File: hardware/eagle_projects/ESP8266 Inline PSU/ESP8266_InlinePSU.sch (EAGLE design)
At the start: 1 part

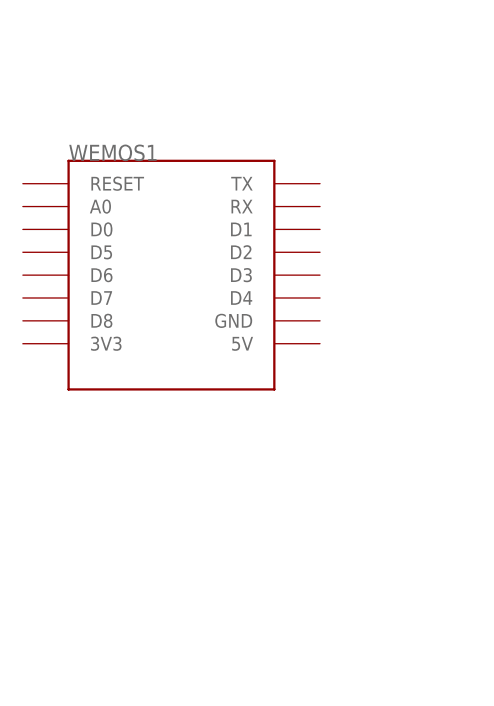
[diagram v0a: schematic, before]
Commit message: Beginning build process for wireless inline PSU and modifications of PSU
Signed-off-by: Braden Licastro <blicastro@live.com>
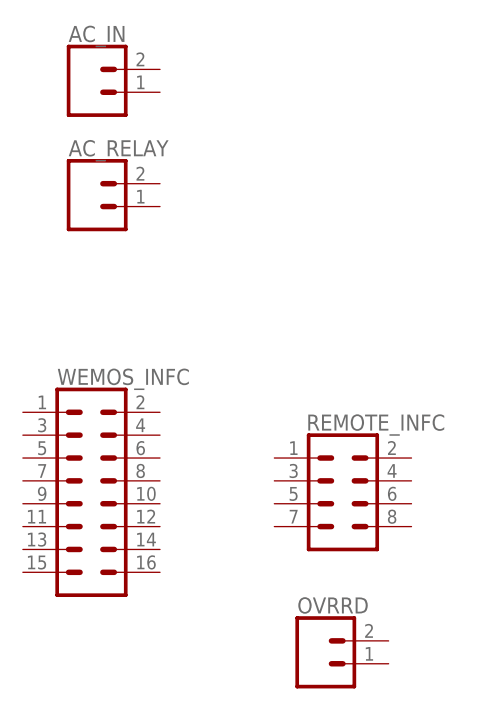
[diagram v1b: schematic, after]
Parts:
- removed WEMOS1: (no value), esp8266modules:WEMOS-D1-MINI
- added AC_IN, AC_RELAY: (no value), SparkFun-Connectors:CONN_023.5MM_LOCK
- added OVRRD: (no value), SparkFun-Connectors:CONN_02LOCK
- added REMOTE_INFC: (no value), SparkFun-Connectors:CONN_04X2
- added WEMOS_INFC: (no value), SparkFun-Connectors:CONN_08X2

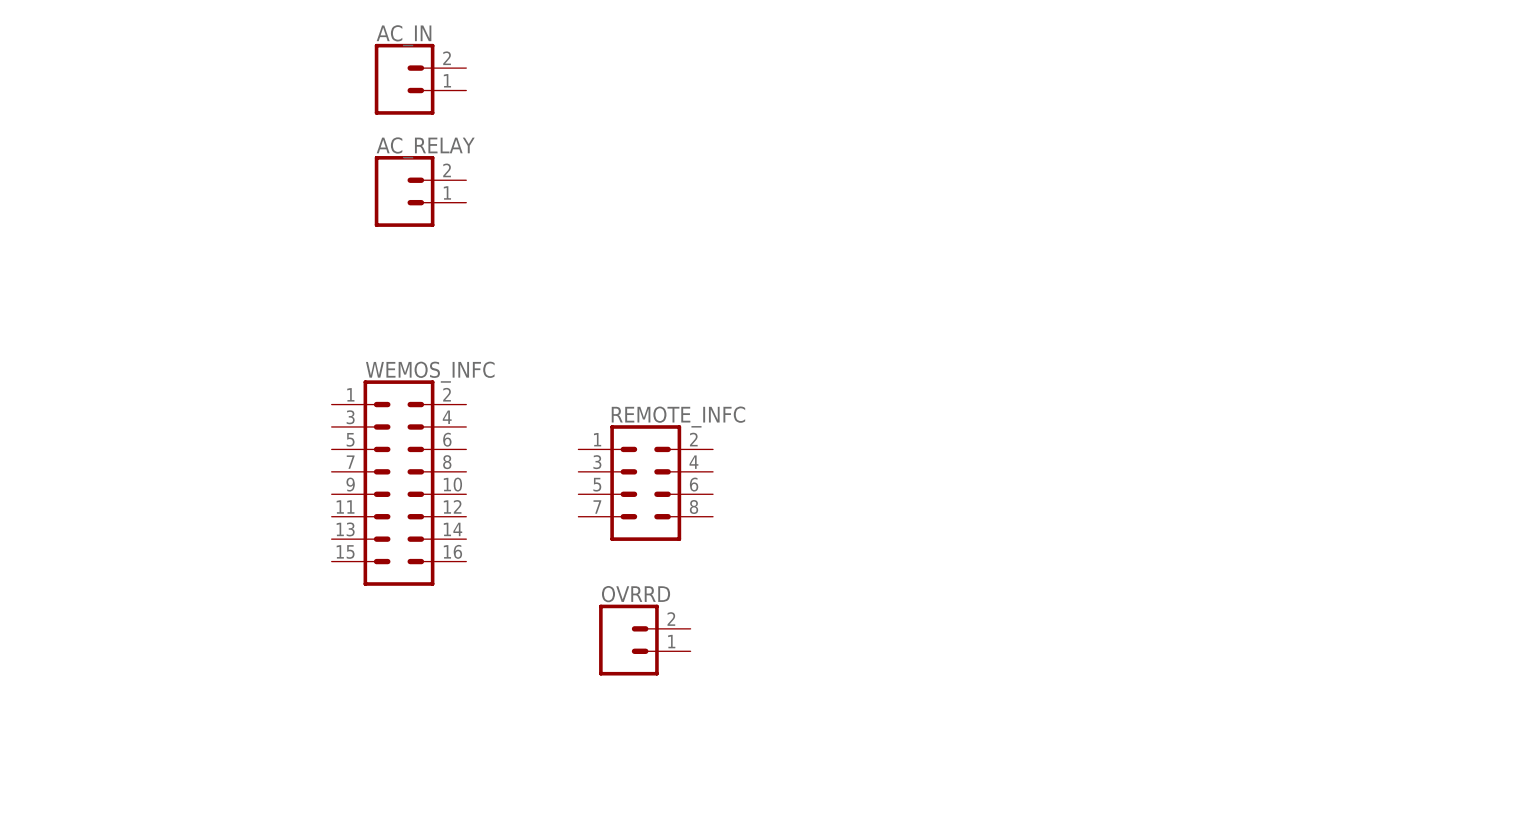
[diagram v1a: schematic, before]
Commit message: Completed more work on hardware design. Broke out sections of sensitive code, optimised existing code. Hacked new device for use and built new firmware. Updated test firmware for deployment on multiple ESP devices.
Signed-off-by: Braden Licastro <blicastro@live.com>
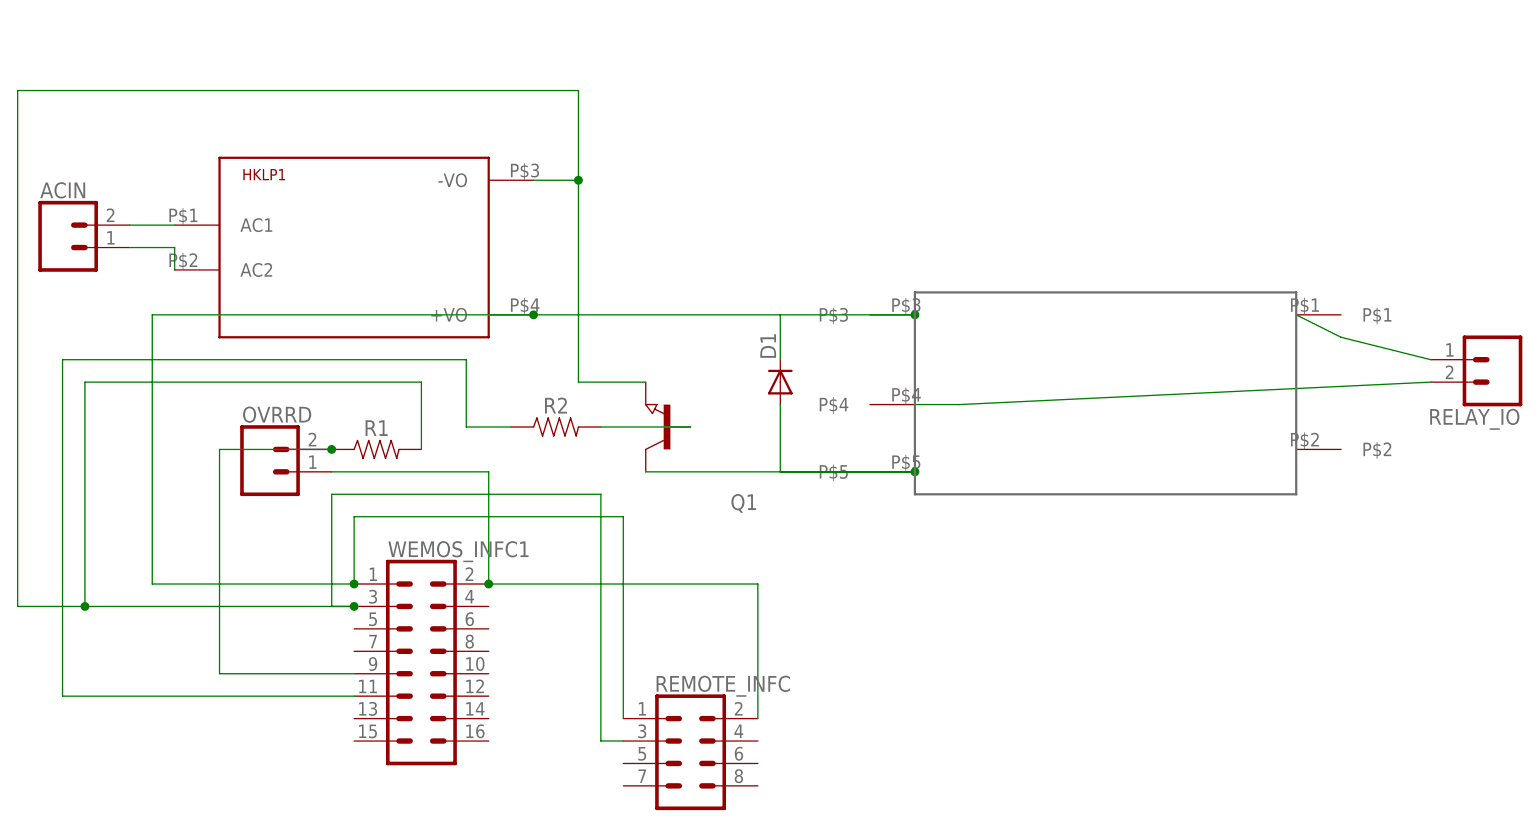
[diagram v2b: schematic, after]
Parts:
- removed AC_IN, AC_RELAY: (no value), SparkFun-Connectors:CONN_023.5MM_LOCK
- removed WEMOS_INFC: (no value), SparkFun-Connectors:CONN_08X2
- added ACIN, RELAY_IO: (no value), SparkFun-Connectors:CONN_025MM
- added D1: 1N4148DO35-7, diode:1N4148DO35-7
- added HKLP1: HKLPM01, bl_components:HKLPM01
- added Q1: (no value), semicon-smd-ipc:NPN-TRANSISTOR_SOT23
- added R1, R2: (no value), SparkFun-Resistors:RESISTOR0805
- added U$1: SRD-05VDC-SL-CTH, bl_components:SRD-05VDC-SL-CTH
- added WEMOS_INFC1: (no value), SparkFun-Connectors:CONN_08X2
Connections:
- new net N$1: ACIN.2, HKLP1.AC1
- new net N$10: Q1.B, R2.2
- new net N$11: R2.1, WEMOS_INFC1.11
- new net N$2: ACIN.1, HKLP1.AC2
- new net N$3: D1.C, HKLP1.+VO, REMOTE_INFC.1, U$1.P$3, WEMOS_INFC1.1
- new net N$4: OVRRD.1, REMOTE_INFC.2, WEMOS_INFC1.2
- new net N$5: HKLP1.-VO, Q1.E, R1.2, REMOTE_INFC.3, WEMOS_INFC1.3
- new net N$6: RELAY_IO.1, U$1.P$1
- new net N$7: RELAY_IO.2, U$1.P$4
- new net N$8: D1.A, Q1.C, U$1.P$5
- new net N$9: OVRRD.2, R1.1, WEMOS_INFC1.9
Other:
- moved on the sheet: OVRRD, REMOTE_INFC
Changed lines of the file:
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@@
 <?xml version="1.0" encoding="utf-8"?>
 <!DOCTYPE eagle SYSTEM "eagle.dtd">
-<eagle version="8.4.0">
+<eagle version="8.4.3">
 <drawing>
 <settings>
@@
 </classes>
 <parts>
-<part name="WEMOS_INFC" library="SparkFun-Connectors" library_urn="urn:adsk.eagle:library:513" deviceset="CONN_08X2" device="" package3d_urn="urn:adsk.eagle:package:38152/1"/>
 <part name="REMOTE_INFC" library="SparkFun-Connectors" library_urn="urn:adsk.eagle:library:513" deviceset="CONN_04X2" device="" package3d_urn="urn:adsk.eagle:package:38103/1"/>
 <part name="OVRRD" library="SparkFun-Connectors" library_urn="urn:adsk.eagle:library:513" deviceset="CONN_02" device="LOCK" package3d_urn="urn:adsk.eagle:package:38045/1"/>
-<part name="AC_IN" library="SparkFun-Connectors" library_urn="urn:adsk.eagle:library:513" deviceset="CONN_02" device="3.5MM_LOCK" package3d_urn="urn:adsk.eagle:package:38049/1"/>
-<part name="AC_RELAY" library="SparkFun-Connectors" library_urn="urn:adsk.eagle:library:513" deviceset="CONN_02" device="3.5MM_LOCK" package3d_urn="urn:adsk.eagle:package:38049/1"/>
+<part name="WEMOS_INFC1" library="SparkFun-Connectors" library_urn="urn:adsk.eagle:library:513" deviceset="CONN_08X2" device="" package3d_urn="urn:adsk.eagle:package:38152/1"/>
+<part name="HKLP1" library="bl_components" deviceset="HKLPM01" device=""/>
+<part name="U$1" library="bl_components" deviceset="SRD-05VDC-SL-C" device="TH"/>
+<part name="RELAY_IO" library="SparkFun-Connectors" library_urn="urn:adsk.eagle:library:513" deviceset="CONN_02" device="5MM" package3d_urn="urn:adsk.eagle:package:38044/1"/>
+<part name="ACIN" library="SparkFun-Connectors" library_urn="urn:adsk.eagle:library:513" deviceset="CONN_02" device="5MM" package3d_urn="urn:adsk.eagle:package:38044/1"/>
+<part name="R1" library="SparkFun-Resistors" deviceset="RESISTOR" device="0805" value=" "/>
+<part name="D1" library="diode" library_urn="urn:adsk.eagle:library:210" deviceset="1N4148" device="DO35-7" package3d_urn="urn:adsk.eagle:package:43339/1"/>
+<part name="Q1" library="semicon-smd-ipc" library_urn="urn:adsk.eagle:library:353" deviceset="NPN-TRANSISTOR_" device="SOT23" package3d_urn="urn:adsk.eagle:package:26310/1"/>
+<part name="R2" library="SparkFun-Resistors" deviceset="RESISTOR" device="0805" value=" "/>
 </parts>
 <sheets>
@@
 </plain>
 <instances>
-<instance part="WEMOS_INFC" gate="G$1" x="78.74" y="45.72"/>
-<instance part="REMOTE_INFC" gate="G$1" x="106.68" y="45.72"/>
-<instance part="OVRRD" gate="G$1" x="104.14" y="27.94"/>
-<instance part="AC_IN" gate="G$1" x="78.74" y="91.44"/>
-<instance part="AC_RELAY" gate="G$1" x="78.74" y="78.74"/>
+<instance part="REMOTE_INFC" gate="G$1" x="111.76" y="15.24"/>
+<instance part="OVRRD" gate="G$1" x="63.5" y="48.26"/>
+<instance part="WEMOS_INFC1" gate="G$1" x="81.28" y="25.4"/>
+<instance part="HKLP1" gate="G$1" x="73.66" y="73.66"/>
+<instance part="U$1" gate="G$1" x="137.16" y="45.72"/>
+<instance part="RELAY_IO" gate="G$1" x="203.2" y="60.96" rot="R180"/>
+<instance part="ACIN" gate="G$1" x="40.64" y="73.66"/>
+<instance part="R1" gate="G$1" x="76.2" y="50.8"/>
+<instance part="D1" gate="G$1" x="121.92" y="58.42" smashed="yes" rot="R90">
+<attribute name="NAME" x="121.4374" y="60.96" size="1.778" layer="95" rot="R90"/>
+</instance>
+<instance part="Q1" gate="G$1" x="109.22" y="53.34" rot="R180"/>
+<instance part="R2" gate="G$1" x="96.52" y="53.34"/>
 </instances>
 <busses>
 </busses>
 <nets>
+<net name="N$1" class="0">
+<segment>
+<pinref part="ACIN" gate="G$1" pin="2"/>
+<pinref part="HKLP1" gate="G$1" pin="AC1"/>
+<wire x1="48.26" y1="76.2" x2="53.34" y2="76.2" width="0.1524" layer="91"/>
+</segment>
+</net>
+<net name="N$2" class="0">
+<segment>
+<pinref part="ACIN" gate="G$1" pin="1"/>
+<pinref part="HKLP1" gate="G$1" pin="AC2"/>
+<wire x1="48.26" y1="73.66" x2="53.34" y2="73.66" width="0.1524" layer="91"/>
+<wire x1="53.34" y1="73.66" x2="53.34" y2="71.12" width="0.1524" layer="91"/>
+</segment>
+</net>
+<net name="N$3" class="0">
+<segment>
+<pinref part="WEMOS_INFC1" gate="G$1" pin="1"/>
+<wire x1="73.66" y1="35.56" x2="73.66" y2="43.18" width="0.1524" layer="91"/>
+<pinref part="REMOTE_INFC" gate="G$1" pin="1"/>
+<wire x1="73.66" y1="43.18" x2="104.14" y2="43.18" width="0.1524" layer="91"/>
+<wire x1="104.14" y1="43.18" x2="104.14" y2="20.32" width="0.1524" layer="91"/>
+<pinref part="HKLP1" gate="G$1" pin="+VO"/>
+<wire x1="93.98" y1="66.04" x2="50.8" y2="66.04" width="0.1524" layer="91"/>
+<wire x1="50.8" y1="66.04" x2="50.8" y2="35.56" width="0.1524" layer="91"/>
+<wire x1="50.8" y1="35.56" x2="73.66" y2="35.56" width="0.1524" layer="91"/>
+<junction x="73.66" y="35.56"/>
+<pinref part="U$1" gate="G$1" pin="P$3"/>
+<wire x1="93.98" y1="66.04" x2="121.92" y2="66.04" width="0.1524" layer="91"/>
+<junction x="93.98" y="66.04"/>
+<pinref part="D1" gate="G$1" pin="C"/>
+<wire x1="137.16" y1="66.04" x2="121.92" y2="66.04" width="0.1524" layer="91"/>
+<wire x1="121.92" y1="66.04" x2="121.92" y2="60.96" width="0.1524" layer="91"/>
+<junction x="137.16" y="66.04"/>
+</segment>
+</net>
+<net name="N$4" class="0">
+<segment>
+<pinref part="WEMOS_INFC1" gate="G$1" pin="2"/>
+<pinref part="REMOTE_INFC" gate="G$1" pin="2"/>
+<wire x1="88.9" y1="35.56" x2="119.38" y2="35.56" width="0.1524" layer="91"/>
+<wire x1="119.38" y1="35.56" x2="119.38" y2="20.32" width="0.1524" layer="91"/>
+<pinref part="OVRRD" gate="G$1" pin="1"/>
+<wire x1="71.12" y1="48.26" x2="88.9" y2="48.26" width="0.1524" layer="91"/>
+<wire x1="88.9" y1="48.26" x2="88.9" y2="35.56" width="0.1524" layer="91"/>
+<junction x="88.9" y="35.56"/>
+</segment>
+</net>
+<net name="N$5" class="0">
+<segment>
+<pinref part="WEMOS_INFC1" gate="G$1" pin="3"/>
+<wire x1="73.66" y1="33.02" x2="71.12" y2="33.02" width="0.1524" layer="91"/>
+<wire x1="71.12" y1="33.02" x2="71.12" y2="45.72" width="0.1524" layer="91"/>
+<wire x1="71.12" y1="45.72" x2="101.6" y2="45.72" width="0.1524" layer="91"/>
+<wire x1="101.6" y1="45.72" x2="101.6" y2="17.78" width="0.1524" layer="91"/>
+<pinref part="REMOTE_INFC" gate="G$1" pin="3"/>
+<wire x1="101.6" y1="17.78" x2="104.14" y2="17.78" width="0.1524" layer="91"/>
+<pinref part="HKLP1" gate="G$1" pin="-VO"/>
+<wire x1="93.98" y1="81.28" x2="99.06" y2="81.28" width="0.1524" layer="91"/>
+<wire x1="99.06" y1="81.28" x2="99.06" y2="91.44" width="0.1524" layer="91"/>
+<wire x1="99.06" y1="91.44" x2="35.56" y2="91.44" width="0.1524" layer="91"/>
+<wire x1="35.56" y1="91.44" x2="35.56" y2="33.02" width="0.1524" layer="91"/>
+<wire x1="35.56" y1="33.02" x2="43.18" y2="33.02" width="0.1524" layer="91"/>
+<junction x="73.66" y="33.02"/>
+<pinref part="R1" gate="G$1" pin="2"/>
+<wire x1="43.18" y1="33.02" x2="73.66" y2="33.02" width="0.1524" layer="91"/>
+<wire x1="81.28" y1="50.8" x2="81.28" y2="58.42" width="0.1524" layer="91"/>
+<wire x1="81.28" y1="58.42" x2="43.18" y2="58.42" width="0.1524" layer="91"/>
+<wire x1="43.18" y1="58.42" x2="43.18" y2="33.02" width="0.1524" layer="91"/>
+<junction x="43.18" y="33.02"/>
+<pinref part="Q1" gate="G$1" pin="E"/>
+<wire x1="106.68" y1="58.42" x2="99.06" y2="58.42" width="0.1524" layer="91"/>
+<wire x1="99.06" y1="58.42" x2="99.06" y2="81.28" width="0.1524" layer="91"/>
+<junction x="99.06" y="81.28"/>
+</segment>
+</net>
+<net name="N$9" class="0">
+<segment>
+<pinref part="OVRRD" gate="G$1" pin="2"/>
+<wire x1="71.12" y1="50.8" x2="58.42" y2="50.8" width="0.1524" layer="91"/>
+<wire x1="58.42" y1="50.8" x2="58.42" y2="25.4" width="0.1524" layer="91"/>
+<pinref part="WEMOS_INFC1" gate="G$1" pin="9"/>
+<wire x1="58.42" y1="25.4" x2="73.66" y2="25.4" width="0.1524" layer="91"/>
+<pinref part="R1" gate="G$1" pin="1"/>
+<junction x="71.12" y="50.8"/>
+</segment>
+</net>
+<net name="N$6" class="0">
+<segment>
+<pinref part="RELAY_IO" gate="G$1" pin="1"/>
+<pinref part="U$1" gate="G$1" pin="P$1"/>
+<wire x1="195.58" y1="60.96" x2="185.42" y2="63.5" width="0.1524" layer="91"/>
+<wire x1="185.42" y1="63.5" x2="180.34" y2="66.04" width="0.1524" layer="91"/>
+</segment>
+</net>
+<net name="N$7" class="0">
+<segment>
+<pinref part="U$1" gate="G$1" pin="P$4"/>
+<pinref part="RELAY_IO" gate="G$1" pin="2"/>
+<wire x1="137.16" y1="55.88" x2="142.24" y2="55.88" width="0.1524" layer="91"/>
+<wire x1="142.24" y1="55.88" x2="195.58" y2="58.42" width="0.1524" layer="91"/>
+</segment>
+</net>
+<net name="N$8" class="0">
+<segment>
+<pinref part="U$1" gate="G$1" pin="P$5"/>
+<pinref part="D1" gate="G$1" pin="A"/>
+<wire x1="137.16" y1="48.26" x2="121.92" y2="48.26" width="0.1524" layer="91"/>
+<wire x1="121.92" y1="48.26" x2="121.92" y2="55.88" width="0.1524" layer="91"/>
+<pinref part="Q1" gate="G$1" pin="C"/>
+<wire x1="106.68" y1="48.26" x2="137.16" y2="48.26" width="0.1524" layer="91"/>
+<junction x="137.16" y="48.26"/>
+</segment>
+</net>
+<net name="N$10" class="0">
+<segment>
+<pinref part="Q1" gate="G$1" pin="B"/>
+<pinref part="R2" gate="G$1" pin="2"/>
+<wire x1="111.76" y1="53.34" x2="101.6" y2="53.34" width="0.1524" layer="91"/>
+</segment>
+</net>
+<net name="N$11" class="0">
+<segment>
+<pinref part="R2" gate="G$1" pin="1"/>
+<wire x1="91.44" y1="53.34" x2="86.36" y2="53.34" width="0.1524" layer="91"/>
+<wire x1="86.36" y1="53.34" x2="86.36" y2="60.96" width="0.1524" layer="91"/>
+<wire x1="86.36" y1="60.96" x2="40.64" y2="60.96" width="0.1524" layer="91"/>
+<wire x1="40.64" y1="60.96" x2="40.64" y2="22.86" width="0.1524" layer="91"/>
+<pinref part="WEMOS_INFC1" gate="G$1" pin="11"/>
+<wire x1="40.64" y1="22.86" x2="73.66" y2="22.86" width="0.1524" layer="91"/>
+</segment>
+</net>
 </nets>
 </sheet>
